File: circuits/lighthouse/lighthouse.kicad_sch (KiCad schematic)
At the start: 40 parts, among them J2 USB_B_Micro, Q1 S9013, Q4 SS8050, Q5 SS8050, U10 CP2102-GMR, U2 AMS1117-3.3, U7 ESP32-WROOM-32

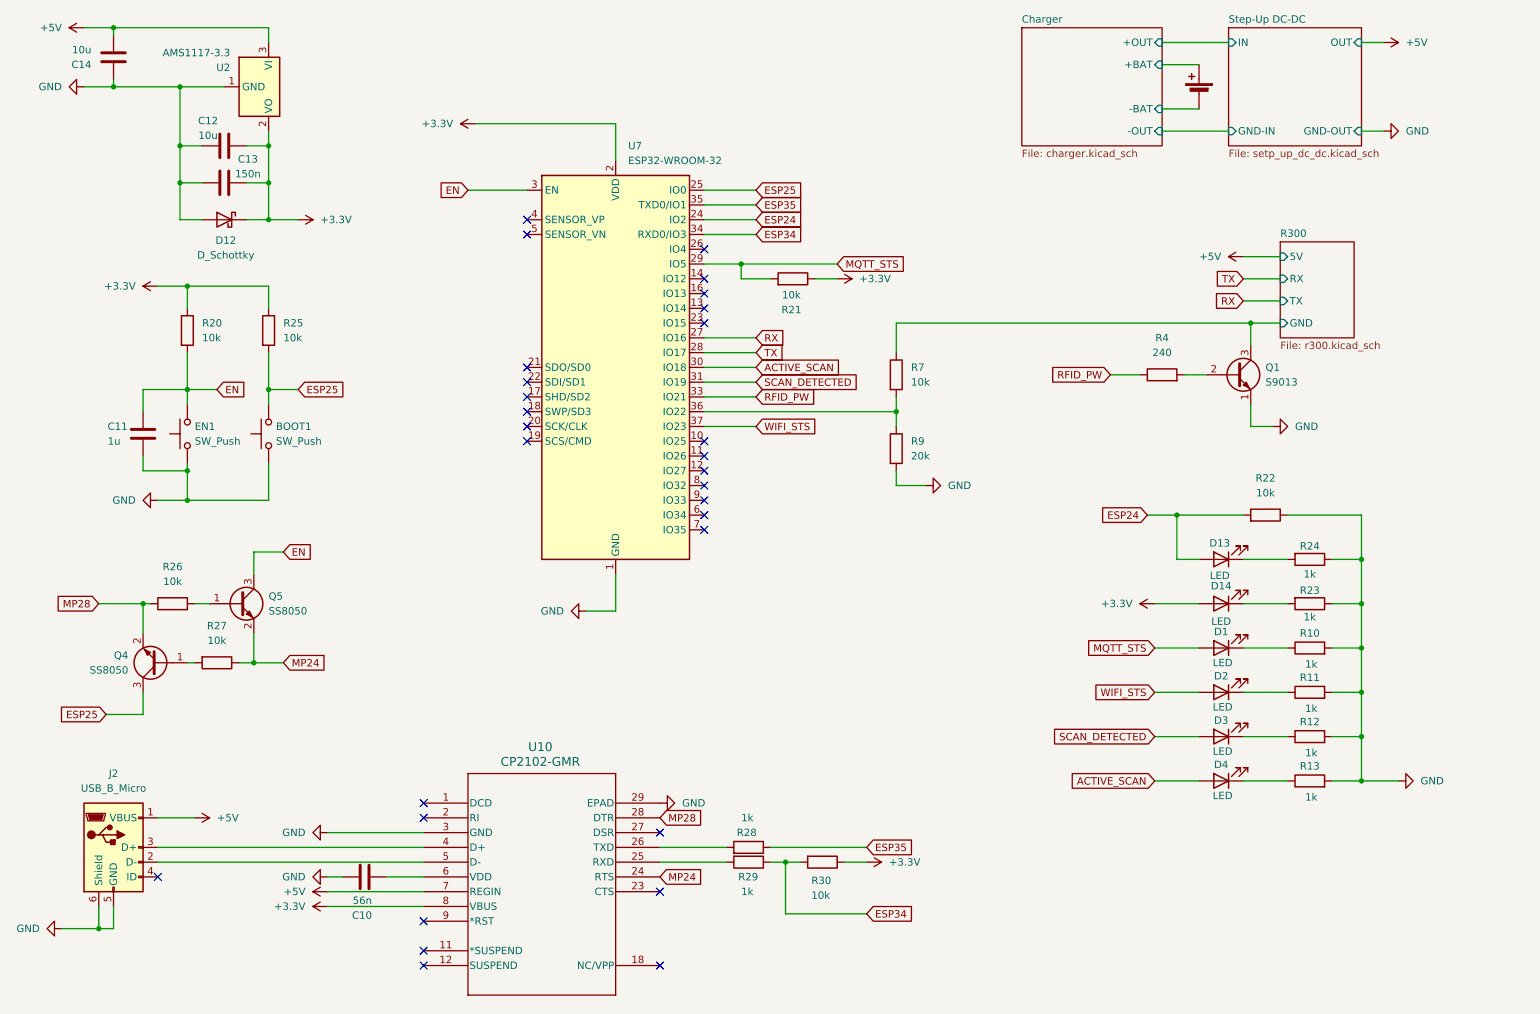
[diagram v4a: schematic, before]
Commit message: Removed one connector from the schematic
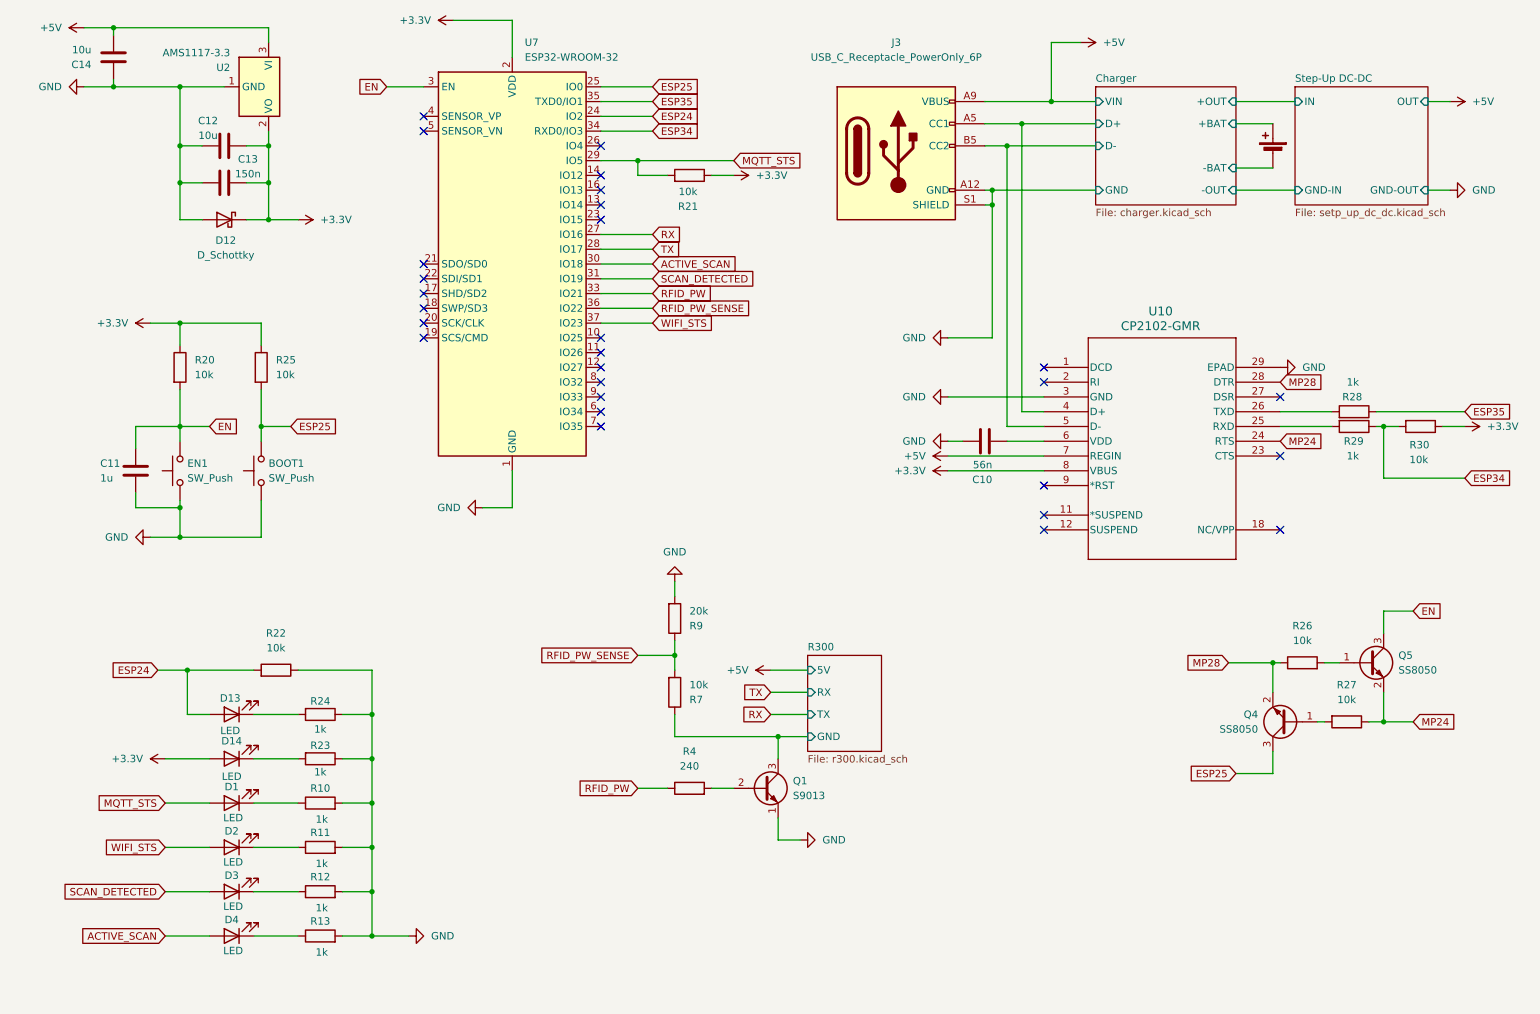
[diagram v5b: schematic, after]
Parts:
- removed J2: USB_B_Micro, Connector_USB:USB_Micro-B_Amphenol_10103594-0001LF_Horizontal, symbol Connector:USB_B_Micro
- added J3: USB_C_Receptacle_PowerOnly_6P, Connector_USB:USB_C_Receptacle_GCT_USB4125-xx-x_6P_TopMnt_Horizontal, symbol Connector:USB_C_Receptacle_PowerOnly_6P
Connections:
- net +5V: now also J3.A9 (VBUS), J3.B9 (VBUS)
- net GND: now also J3.A12 (GND), J3.B12 (GND), J3.S1 (SHIELD)
- net RFID_PW_SENSE: now reaches R7.2, R9.1, U7.36 (IO22)
- net Charger/D+: now reaches U10.4 (D+)
- net Charger/D+: now also J3.A5 (CC1)
- net Charger/D-: now reaches U10.5 (D-)
- net Charger/D-: now also J3.B5 (CC2)
- no-connect marks 29 -> 28
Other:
- sheet Charger ports: added D+, D-, GND, VIN; removed none
- moved on the sheet: BOOT1, C10, C11, D1, D13, D14, D2, D3, D4, EN1, Q1, Q4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
